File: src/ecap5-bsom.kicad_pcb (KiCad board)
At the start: 6 copper layers, 69.6 x 30 mm, 191 parts, among them J13 DDR4_SODIMM_Board, U1 TPS565242DRDR, U10 IS42S16160J-*BL, U11 IS43DR86400E, U12 ASFC4G31M-51*, U2 TPS562202DRLR, U3 TPS562202DRLR, U4 TPS562202DRLR, U5 LM3880MF*-1AA, U6 LFE5U-85F-*BG756*, U7 XLH335040.000000I, U8 W25Q128JVPIQ, U9 IS61WV25616BLL-*BLI

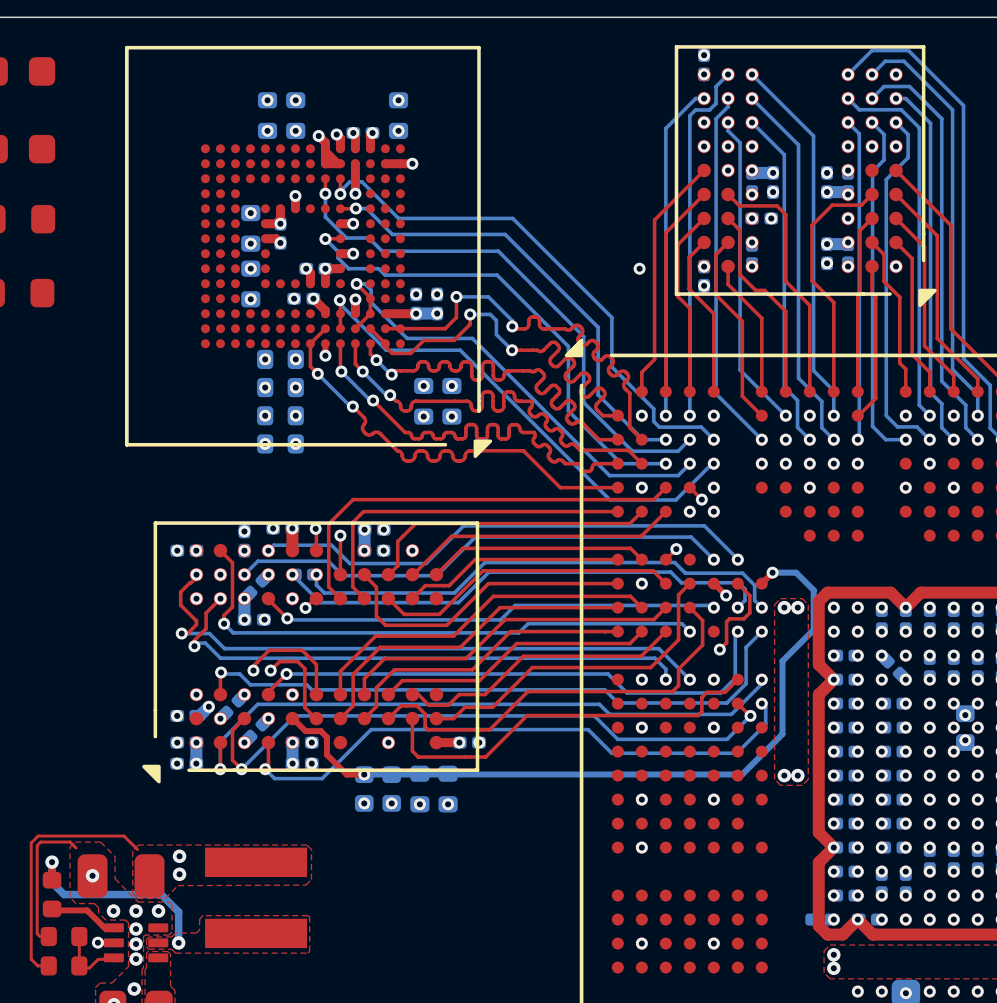
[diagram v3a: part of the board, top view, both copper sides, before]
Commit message: Update routing of emmc
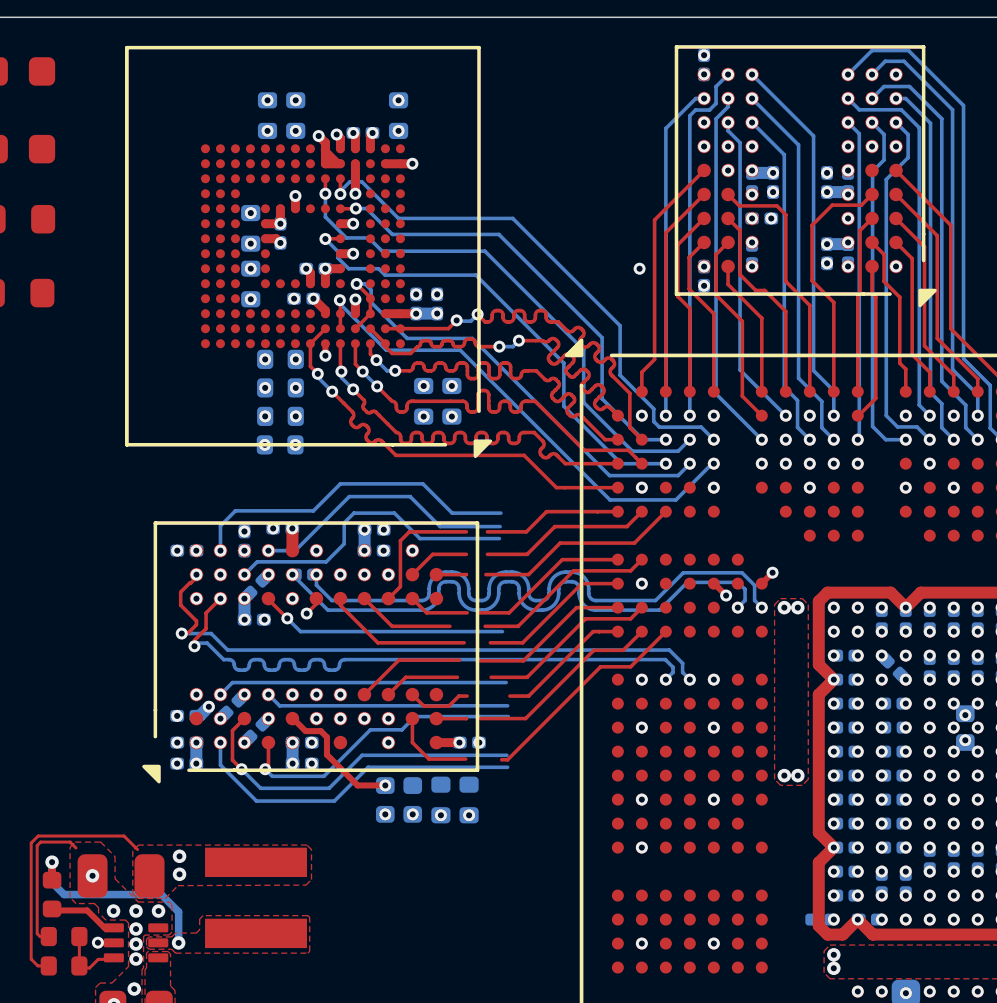
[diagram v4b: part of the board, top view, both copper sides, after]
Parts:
- moved R2 1.91 mm to (106.4, 39.3)
- moved R38 1.87 mm to (106.4, 37.4)
- moved C121 0.79 mm to (110.8, 51.2)
- moved C138 0.79 mm to (109.9, 51.2)
- moved R23 0.79 mm to (112.7, 51.2)
- moved R24 0.79 mm to (111.8, 51.2)
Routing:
- net /DDR2/VREF: track 25.3 -> 4.85 mm
- net /FPGA Bank 7/DDR2.CKE: track 21.5 -> 5.79 mm, vias 2 -> 1
- net /FPGA Bank 7/DDR2.~{WE}: track 20.5 -> 5.74 mm, vias 2 -> 1
- net /DDR2/A3: track 14.1 -> 2.73 mm, vias 0 -> 1
- net /FPGA Bank 7/DDR2.DM: track 20.9 -> 9.69 mm, vias 2 -> 1
- net /DDR2/A7: track 13.4 -> 2.80 mm
- net /DDR2/A12: track 11.2 -> 1.00 mm
- net /DDR2/DQ4: track 19.9 -> 9.96 mm, vias 2 -> 1
- net /FPGA Bank 7/~{RAS}: track 15.4 -> 5.56 mm, vias 2 -> 1
- net /DDR2/DQ6: track 21.1 -> 11.3 mm, vias 2 -> 1
- net /DDR2/DQ3: track 17.9 -> 8.13 mm, vias 2 -> 1
- net /FPGA Bank 7/DDR2.~{CAS}: track 14.4 -> 4.87 mm
- net /DDR2/DQ1: track 20.9 -> 11.5 mm, vias 2 -> 1
- net /FPGA Bank 7/DDR2.~{CS}: track 13.3 -> 4.42 mm, vias 2 -> 1
- net /FPGA Bank 7/DDR2.ODT: track 14.6 -> 5.81 mm, vias 2 -> 1
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
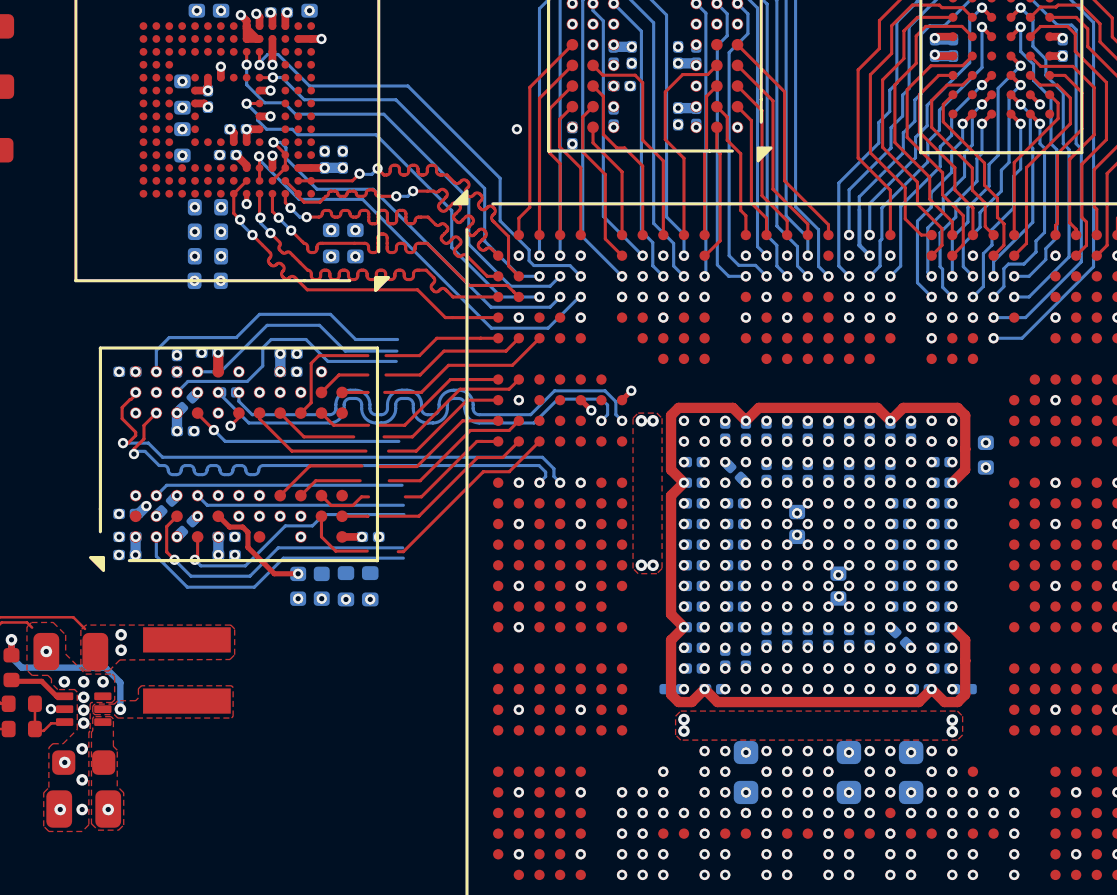
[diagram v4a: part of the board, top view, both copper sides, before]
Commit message: Route the DDR2 without length matching
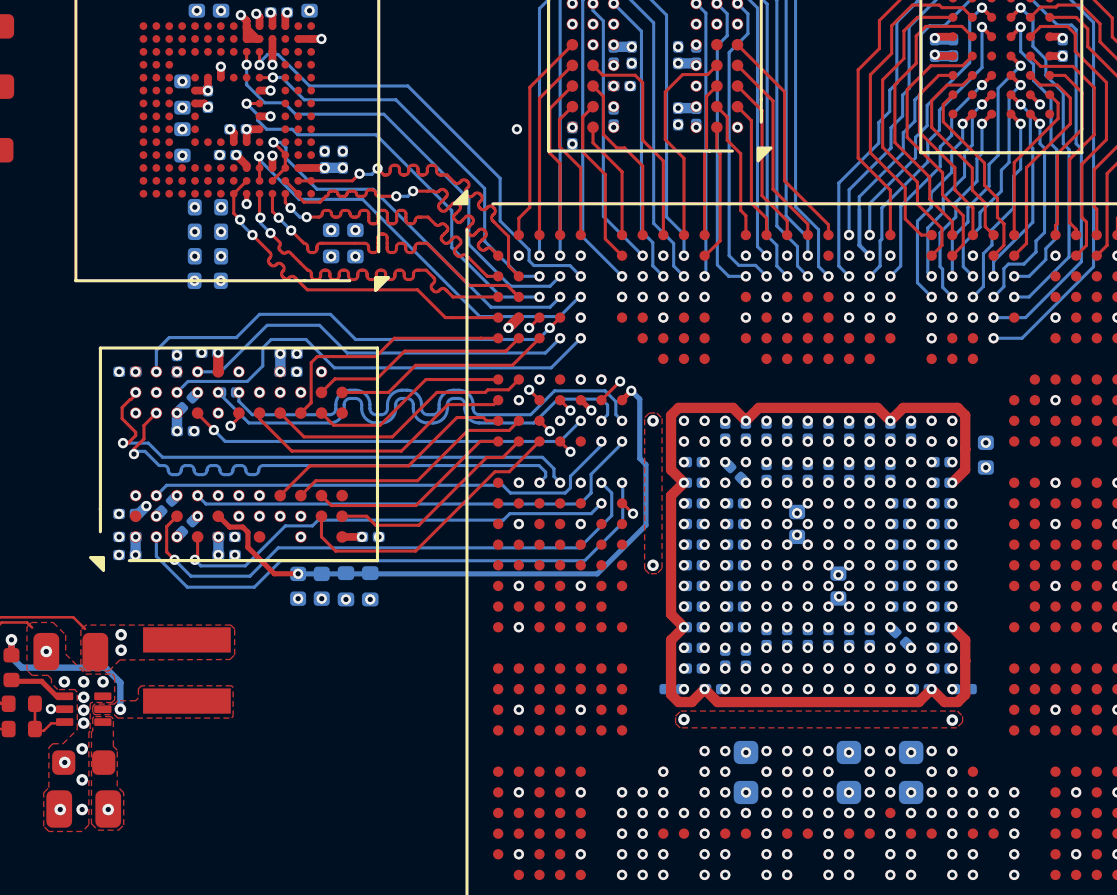
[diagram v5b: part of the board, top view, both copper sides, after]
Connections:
- U11 pad F7: /FPGA Bank 7/~{RAS} -> /FPGA Bank 7/DDR2.~{RAS}
- U6 pad E3: /FPGA Bank 7/DDR2.~{CAS} -> /FPGA Bank 7/DDR2.ODT
- U6 pad E4: /FPGA Bank 7/DDR2.ODT -> /DDR2/DQ7
- U6 pad F1: /DDR2/A1 -> /DDR2/A6
- U6 pad F2: /DDR2/A4 -> /DDR2/A8
- U6 pad F3: /DDR2/A8 -> /DDR2/A13
- U6 pad F4: /FPGA Bank 7/DDR2.~{CS} -> /DDR2/DQ5
- U6 pad F5: /FPGA Bank 7/~{RAS} -> /DDR2/DQ0
- U6 pad H2: /DDR2/A13 -> /DDR2/A1
- U6 pad H3: /FPGA Bank 7/DDR2.~{WE} -> /FPGA Bank 7/DDR2.~{CS}
- U6 pad H5: /DDR2/DQ0 -> /DDR2/A4
- U6 pad H6: /DDR2/DQ5 -> /DDR2/A0
- U6 pad J1: /DDR2/A0 -> /FPGA Bank 7/DDR2.~{CAS}
- U6 pad J3: /DDR2/A6 -> /FPGA Bank 7/DDR2.~{RAS}
- U6 pad J4: /DDR2/A12 -> /FPGA Bank 7/DDR2.CKE
- U6 pad J6: /FPGA Bank 7/DDR2.CKE -> /FPGA Bank 7/DDR2.~{WE}
- U6 pad K1: /DDR2/BA0 -> /DDR2/A2
- U6 pad K2: /DDR2/BA1 -> /DDR2/A5
- U6 pad K3: /DDR2/A2 -> /DDR2/BA1
- U6 pad K4: /DDR2/A3 -> /DDR2/A10
- U6 pad L1: /DDR2/A10 -> /DDR2/A9
- U6 pad L2: /DDR2/A5 -> /DDR2/A12
- U6 pad L3: /DDR2/A9 -> /DDR2/A7
- U6 pad L4: /DDR2/DQ7 -> /DDR2/A3
- U6 pad L6: /DDR2/DQ3 -> /FPGA Bank 7/DDR2.DM
- U6 pad L7: /FPGA Bank 7/DDR2.DM -> /DDR2/DQ3
- U6 pad N6: /DDR2/A7 -> /DDR2/DQ1
- U6 pad P6: /DDR2/DQ1 -> /DDR2/DQ4
- U6 pad P7: /DDR2/DQ4 -> /DDR2/BA0
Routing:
- net /DDR2/VREF: track 4.85 -> 24.6 mm
- net /FPGA Bank 7/DDR2.~{RAS}: track 0.00 -> 13.4 mm, vias 0 -> 2
- net /FPGA Bank 7/DDR2.~{WE}: track 5.74 -> 18.2 mm, vias 1 -> 2
- net /DDR2/DQ6: track 11.3 -> 21.9 mm, vias 1 -> 2
- net /DDR2/A3: track 2.73 -> 13.2 mm, vias 1 -> 2
- net /DDR2/DQ1: track 11.5 -> 21.6 mm, vias 1 -> 2
- net /DDR2/DQ3: track 8.13 -> 18.1 mm, vias 1 -> 2
- net /FPGA Bank 7/DDR2.CKE: track 5.79 -> 15.6 mm, vias 1 -> 2
- net /FPGA Bank 7/DDR2.DM: track 9.69 -> 18.7 mm, vias 1 -> 2
- net /DDR2/A7: track 2.80 -> 11.2 mm
- net /DDR2/DQ4: track 9.96 -> 17.8 mm, vias 1 -> 2
- net /DDR2/DQ0: track 10.1 -> 17.8 mm, vias 1 -> 2
- net /DDR2/DQ2: track 8.24 -> 15.6 mm, vias 1 -> 2
- net /DDR2/A12: track 1.00 -> 8.34 mm
- net /FPGA Bank 7/DDR2.~{CS}: track 4.42 -> 11.7 mm, vias 1 -> 2
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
